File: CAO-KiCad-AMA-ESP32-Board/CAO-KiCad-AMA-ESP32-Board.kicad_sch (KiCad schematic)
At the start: 86 parts, among them J13 DHT Sensor, J14 Pot, J15 Select A, J16 Select B, J17 I2C, J3 Conn_01x19, J4 Conn_01x19, J5 Micro_SD_Card, J6 Servo, J7 I2C, J8 5V Ext, Q1 IRLML6402, SW1 SW_Push, SW2 SW_Push, SW3 SW_Push, SW4 SW_Push, SW5 SW_Push, SW6 SW_Push, U1 ESP32-DevKitC, U2 74HC595, Y1 Crystal_GND3_Small

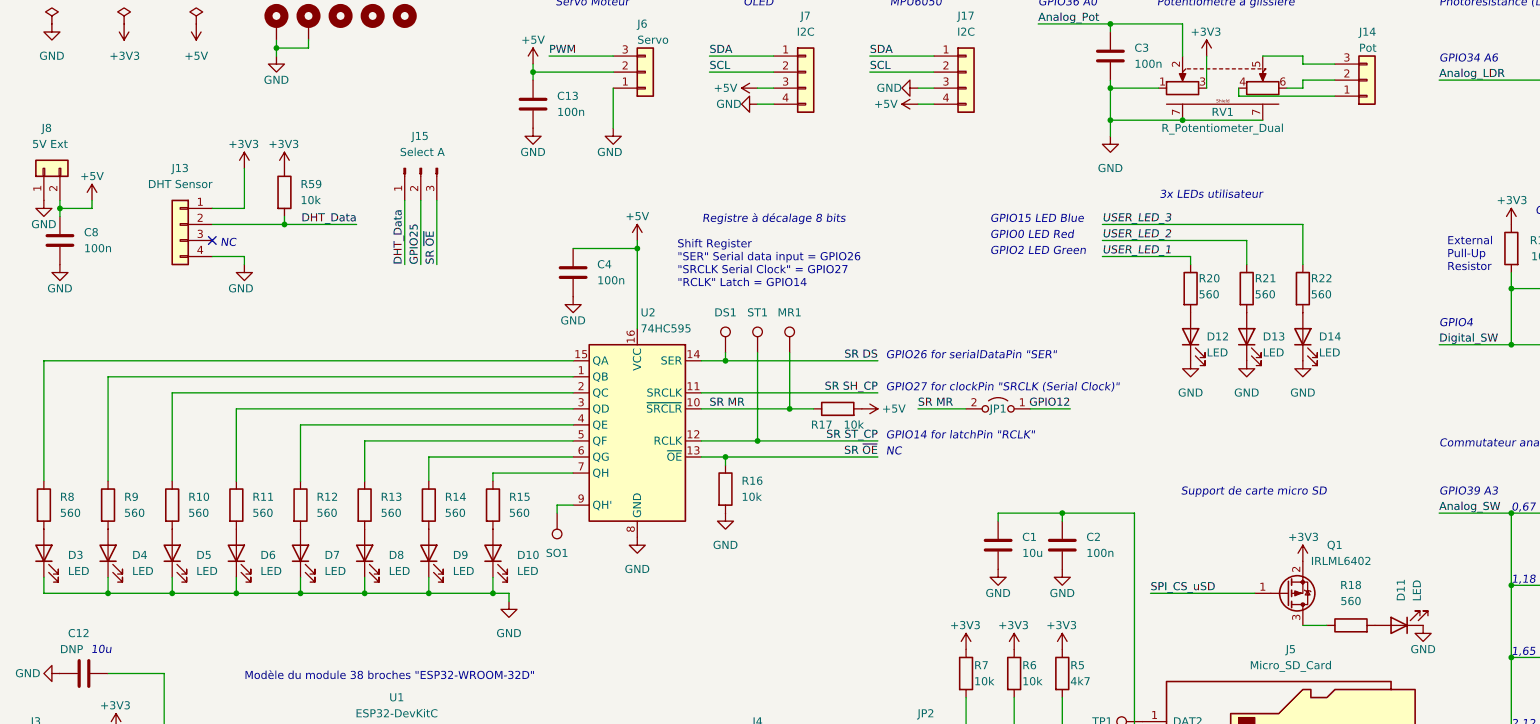
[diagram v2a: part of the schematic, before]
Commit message: MAJ valeurs R pour LEDs
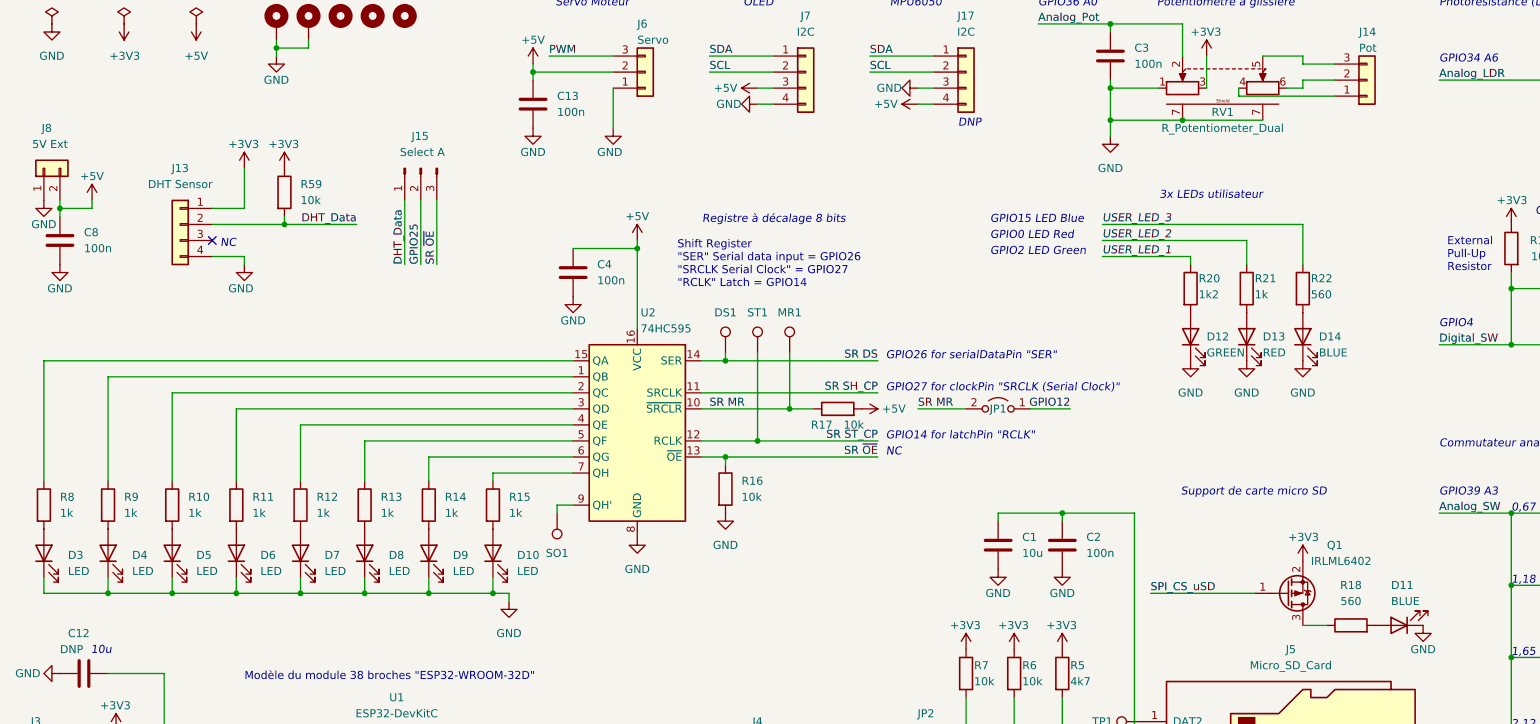
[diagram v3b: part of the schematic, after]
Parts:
- D11, D14: value LED -> BLUE
- D12: value LED -> GREEN
- D13: value LED -> RED
- R10, R11, R12, R13, R14, R15, R21, R8, R9: value 560 -> 1k
- R20: value 560 -> 1k2
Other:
- note added: "DNP"
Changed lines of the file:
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@@
+    (effects (font (size 1.27 1.27) italic) (justify left bottom))
+  )
+  (text "DNP" (at 165.1 39.37 0)
     (effects (font (size 1.27 1.27) italic) (justify left bottom))
   )
@@
       (effects (font (size 1.27 1.27)) (justify left))
     )
-    (property "Value" "560" (id 1) (at 63.5 100.3299 0)
+    (property "Value" "1k" (id 1) (at 63.5 100.3299 0)
       (effects (font (size 1.27 1.27)) (justify left))
     )
@@
       (effects (font (size 1.27 1.27)) (justify left))
     )
-    (property "Value" "560" (id 1) (at 43.18 100.3299 0)
+    (property "Value" "1k" (id 1) (at 43.18 100.3299 0)
       (effects (font (size 1.27 1.27)) (justify left))
     )
@@
       (effects (font (size 1.27 1.27)) (justify left))
     )
-    (property "Value" "560" (id 1) (at 33.02 100.3299 0)
+    (property "Value" "1k" (id 1) (at 33.02 100.3299 0)
       (effects (font (size 1.27 1.27)) (justify left))
     )
@@
       (effects (font (size 1.27 1.27)) (justify right))
     )
-    (property "Value" "LED" (id 1) (at 204.47 74.93 90)
+    (property "Value" "GREEN" (id 1) (at 204.47 74.93 90)
       (effects (font (size 1.27 1.27)) (justify right))
     )
@@
       (effects (font (size 1.27 1.27)) (justify left))
     )
-    (property "Value" "560" (id 1) (at 22.86 100.3299 0)
+    (property "Value" "1k" (id 1) (at 22.86 100.3299 0)
       (effects (font (size 1.27 1.27)) (justify left))
     )
@@
       (effects (font (size 1.27 1.27)) (justify right))
     )
-    (property "Value" "LED" (id 1) (at 213.36 74.93 90)
+    (property "Value" "RED" (id 1) (at 213.36 74.93 90)
       (effects (font (size 1.27 1.27)) (justify right))
     )
@@
       (effects (font (size 1.27 1.27)) (justify left))
     )
-    (property "Value" "560" (id 1) (at 203.2 65.7225 0)
+    (property "Value" "1k2" (id 1) (at 203.2 65.7225 0)
       (effects (font (size 1.27 1.27)) (justify left))
     )
@@
       (effects (font (size 1.27 1.27)) (justify left))
     )
-    (property "Value" "560" (id 1) (at 83.82 100.3299 0)
+    (property "Value" "1k" (id 1) (at 83.82 100.3299 0)
       (effects (font (size 1.27 1.27)) (justify left))
     )
@@
       (effects (font (size 1.27 1.27)) (justify left))
     )
-    (property "Value" "560" (id 1) (at 53.34 100.3299 0)
+    (property "Value" "1k" (id 1) (at 53.34 100.3299 0)
       (effects (font (size 1.27 1.27)) (justify left))
     )
@@
   )
   (symbol (lib_id "Device:LED") (at 234.95 118.11 180) (unit 1)
-    (in_bom yes) (on_board yes) (fields_autoplaced)
-    (property "Reference" "D11" (id 0) (at 235.2674 114.3 90)
-      (effects (font (size 1.27 1.27)) (justify right))
-    )
-    (property "Value" "LED" (id 1) (at 237.8074 114.3 90)
+    (in_bom yes) (on_board yes)
+    (property "Reference" "D11" (id 0) (at 233.68 111.76 0)
+      (effects (font (size 1.27 1.27)) (justify right))
+    )
+    (property "Value" "BLUE" (id 1) (at 233.68 114.3 0)
       (effects (font (size 1.27 1.27)) (justify right))
     )
@@
       (effects (font (size 1.27 1.27)) (justify right))
     )
-    (property "Value" "LED" (id 1) (at 222.25 74.93 90)
+    (property "Value" "BLUE" (id 1) (at 222.25 74.93 90)
       (effects (font (size 1.27 1.27)) (justify right))
     )
@@
       (effects (font (size 1.27 1.27)) (justify left))
     )
-    (property "Value" "560" (id 1) (at 212.09 65.7225 0)
+    (property "Value" "1k" (id 1) (at 212.09 65.7225 0)
       (effects (font (size 1.27 1.27)) (justify left))
     )
@@
       (effects (font (size 1.27 1.27)) (justify left))
     )
-    (property "Value" "560" (id 1) (at 73.66 100.3299 0)
+    (property "Value" "1k" (id 1) (at 73.66 100.3299 0)
       (effects (font (size 1.27 1.27)) (justify left))
     )
@@
       (effects (font (size 1.27 1.27)) (justify left))
     )
-    (property "Value" "560" (id 1) (at 93.98 100.3299 0)
+    (property "Value" "1k" (id 1) (at 93.98 100.3299 0)
       (effects (font (size 1.27 1.27)) (justify left))
     )
@@
     )
     (path "/99b24f75-ab71-4ebe-9160-f6a192899fad"
-      (reference "D11") (unit 1) (value "LED") (footprint "LED_SMD:LED_0603_1608Metric_Pad1.05x0.95mm_HandSolder")
+      (reference "D11") (unit 1) (value "BLUE") (footprint "LED_SMD:LED_0603_1608Metric_Pad1.05x0.95mm_HandSolder")
     )
     (path "/2aea5a5a-4bfb-4f34-a2a8-9d07c991529a"
-      (reference "D12") (unit 1) (value "LED") (footprint "LED_SMD:LED_0805_2012Metric_Pad1.15x1.40mm_HandSolder")
+      (reference "D12") (unit 1) (value "GREEN") (footprint "LED_SMD:LED_0805_2012Metric_Pad1.15x1.40mm_HandSolder")
     )
     (path "/609894d3-d451-4e21-83eb-f74fdcad7192"
-      (reference "D13") (unit 1) (value "LED") (footprint "LED_SMD:LED_0805_2012Metric_Pad1.15x1.40mm_HandSolder")
+      (reference "D13") (unit 1) (value "RED") (footprint "LED_SMD:LED_0805_2012Metric_Pad1.15x1.40mm_HandSolder")
     )
     (path "/c5ac53b2-3445-4c24-a01a-544e650a91eb"
-      (reference "D14") (unit 1) (value "LED") (footprint "LED_SMD:LED_0805_2012Metric_Pad1.15x1.40mm_HandSolder")
+      (reference "D14") (unit 1) (value "BLUE") (footprint "LED_SMD:LED_0805_2012Metric_Pad1.15x1.40mm_HandSolder")
     )
     (path "/8db0b998-7797-49c6-b7a1-144a4c202ed6"
@@
     )
     (path "/2e74c563-5b0b-43e6-b7a9-70d6f498bd02"
-      (reference "R8") (unit 1) (value "560") (footprint "Resistor_SMD:R_0805_2012Metric_Pad1.20x1.40mm_HandSolder")
+      (reference "R8") (unit 1) (value "1k") (footprint "Resistor_SMD:R_0805_2012Metric_Pad1.20x1.40mm_HandSolder")
     )
     (path "/20ff6ca3-d0c8-4a3d-a4eb-7a679cdfe9ff"
-      (reference "R9") (unit 1) (value "560") (footprint "Resistor_SMD:R_0805_2012Metric_Pad1.20x1.40mm_HandSolder")
+      (reference "R9") (unit 1) (value "1k") (footprint "Resistor_SMD:R_0805_2012Metric_Pad1.20x1.40mm_HandSolder")
     )
     (path "/1ce5a473-f094-4292-ad32-bf810073f292"
-      (reference "R10") (unit 1) (value "560") (footprint "Resistor_SMD:R_0805_2012Metric_Pad1.20x1.40mm_HandSolder")
+      (reference "R10") (unit 1) (value "1k") (footprint "Resistor_SMD:R_0805_2012Metric_Pad1.20x1.40mm_HandSolder")
     )
     (path "/94749e15-59bd-4e71-8f96-138cc034620f"
-      (reference "R11") (unit 1) (value "560") (footprint "Resistor_SMD:R_0805_2012Metric_Pad1.20x1.40mm_HandSolder")
+      (reference "R11") (unit 1) (value "1k") (footprint "Resistor_SMD:R_0805_2012Metric_Pad1.20x1.40mm_HandSolder")
     )
     (path "/12933eac-62b4-44dd-8c4e-5d69687afdf2"
-      (reference "R12") (unit 1) (value "560") (footprint "Resistor_SMD:R_0805_2012Metric_Pad1.20x1.40mm_HandSolder")
+      (reference "R12") (unit 1) (value "1k") (footprint "Resistor_SMD:R_0805_2012Metric_Pad1.20x1.40mm_HandSolder")
     )
     (path "/d4864835-3bd1-4dd5-8072-bf1fd39d0535"
-      (reference "R13") (unit 1) (value "560") (footprint "Resistor_SMD:R_0805_2012Metric_Pad1.20x1.40mm_HandSolder")
+      (reference "R13") (unit 1) (value "1k") (footprint "Resistor_SMD:R_0805_2012Metric_Pad1.20x1.40mm_HandSolder")
     )
     (path "/924157b6-61e7-4b28-bcdd-59736f754737"
-      (reference "R14") (unit 1) (value "560") (footprint "Resistor_SMD:R_0805_2012Metric_Pad1.20x1.40mm_HandSolder")
+      (reference "R14") (unit 1) (value "1k") (footprint "Resistor_SMD:R_0805_2012Metric_Pad1.20x1.40mm_HandSolder")
     )
     (path "/ec223fcc-f850-4e54-8a6c-d919c01551ab"
-      (reference "R15") (unit 1) (value "560") (footprint "Resistor_SMD:R_0805_2012Metric_Pad1.20x1.40mm_HandSolder")
+      (reference "R15") (unit 1) (value "1k") (footprint "Resistor_SMD:R_0805_2012Metric_Pad1.20x1.40mm_HandSolder")
     )
     (path "/5bc8af2f-09f0-4918-a8f0-b0918f9812ff"
@@
     )
     (path "/6c2a20d2-a082-48d5-bf8b-cf6b8b3966f8"
-      (reference "R20") (unit 1) (value "560") (footprint "Resistor_SMD:R_0805_2012Metric_Pad1.20x1.40mm_HandSolder")
+      (reference "R20") (unit 1) (value "1k2") (footprint "Resistor_SMD:R_0805_2012Metric_Pad1.20x1.40mm_HandSolder")
     )
     (path "/d2770d8c-4165-423c-9cd0-01736ae6df0f"
-      (reference "R21") (unit 1) (value "560") (footprint "Resistor_SMD:R_0805_2012Metric_Pad1.20x1.40mm_HandSolder")
+      (reference "R21") (unit 1) (value "1k") (footprint "Resistor_SMD:R_0805_2012Metric_Pad1.20x1.40mm_HandSolder")
     )
     (path "/b4043597-e8f7-4bd2-88d4-cee2c66e5b18"
